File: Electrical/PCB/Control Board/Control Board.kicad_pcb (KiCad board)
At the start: 2 copper layers, 154 x 175 mm, 92 parts, among them J1 ED2627-ND, J10 6posheader, J11 S7038-ND, J13 ED1501-ND, J14 ED2989-ND-USB, J15 ED2580-ND, J16 ED2580-ND, J17 ED2744-ND, J18 ED2744-ND, J19 ED2744-ND, J2 ED2627-ND, J20 ED2744-ND, J21 ED2744-ND, J22 ED2744-ND, J23 ED2744-ND, J24 ED2744-ND, J25 ED2744-ND, J26 ED2744-ND, J28 ED2580-ND, J29 ED2580-ND, J3 ED2627-ND, J30 ED2580-ND, J31 ED2580-ND, J4 ED2627-ND, J5 ED2627-ND, J6 S9175-ND, J7 S9175-ND, J8 6posheader, J9 S7038-ND, M1 Mounting_Holes, T1 test_point, T10 test_point, T11 test_point, T12 test_point, T13 test_point, T14 test_point, T15 test_point, T16 test_point, T17 test_point, T18 test_point, T19 test_point, T2 test_point, T20 test_point, T21 test_point, T3 test_point, T4 test_point, T5 test_point, T6 test_point, T7 test_point, T8 test_point, T9 test_point, U1 LM358-N, U2 LM358-N, y1 rover_silkscreen

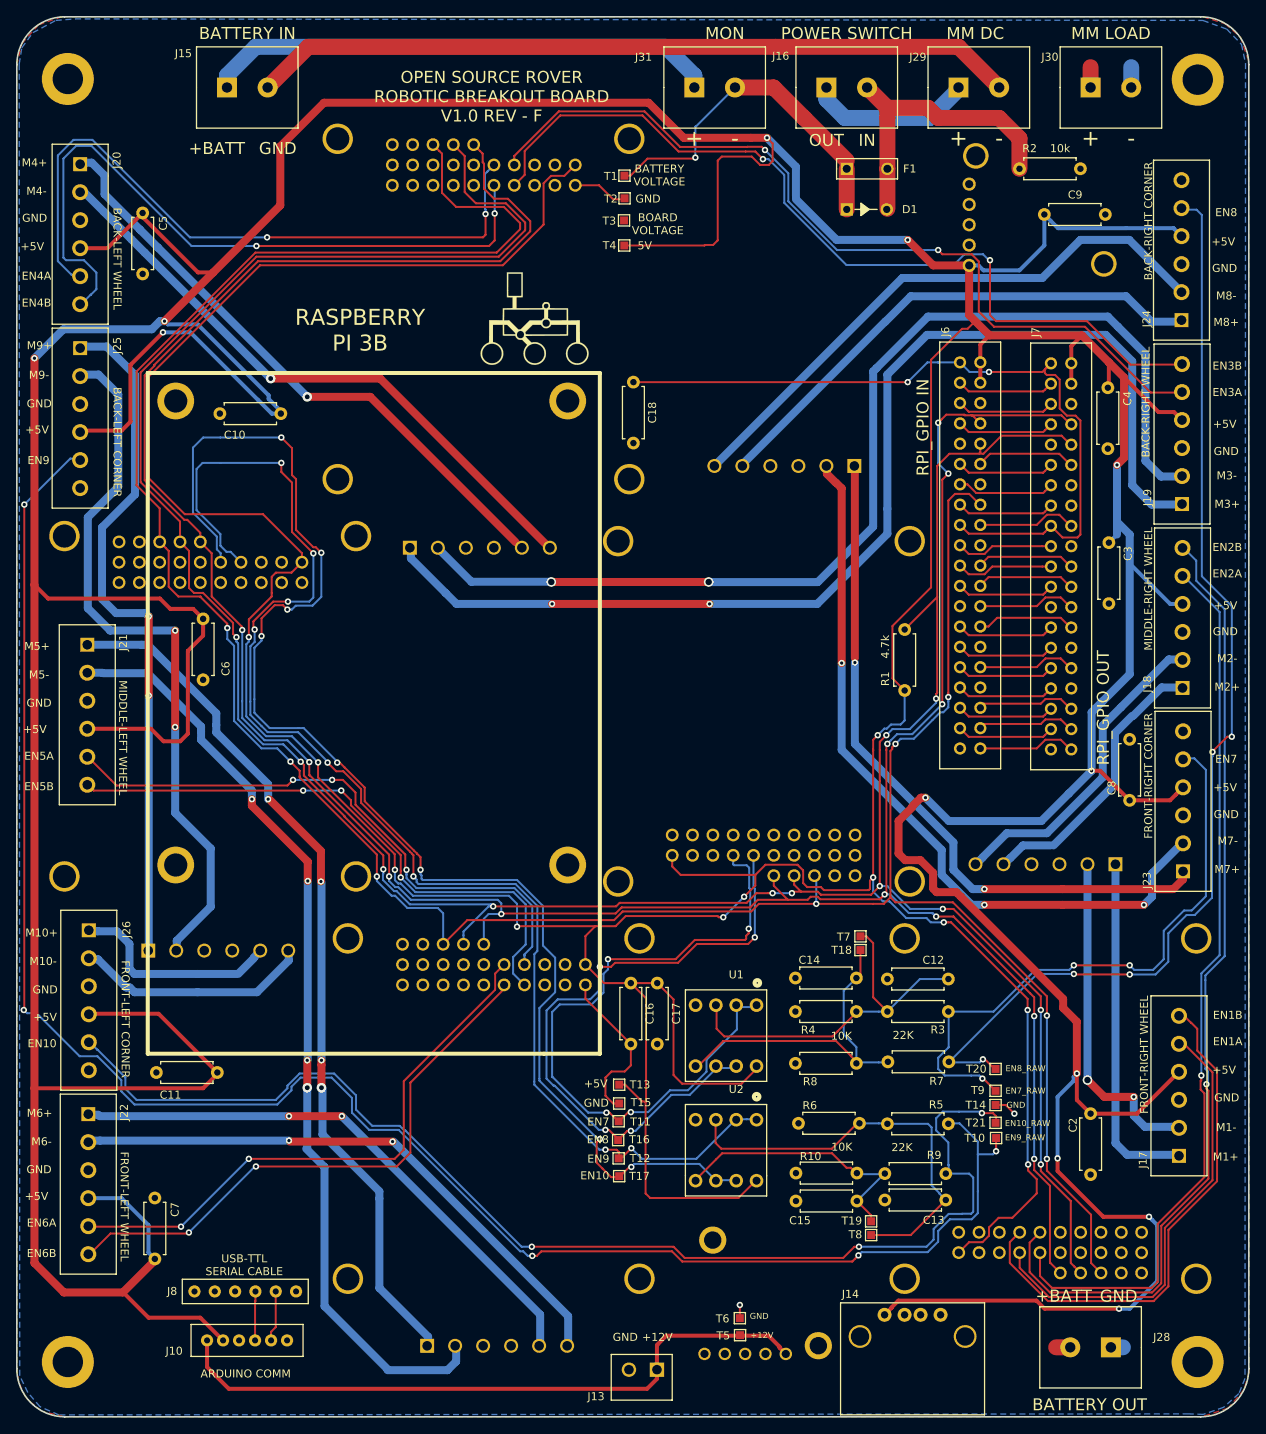
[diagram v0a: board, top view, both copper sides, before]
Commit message: Added filter caps for quadrature encoder signals
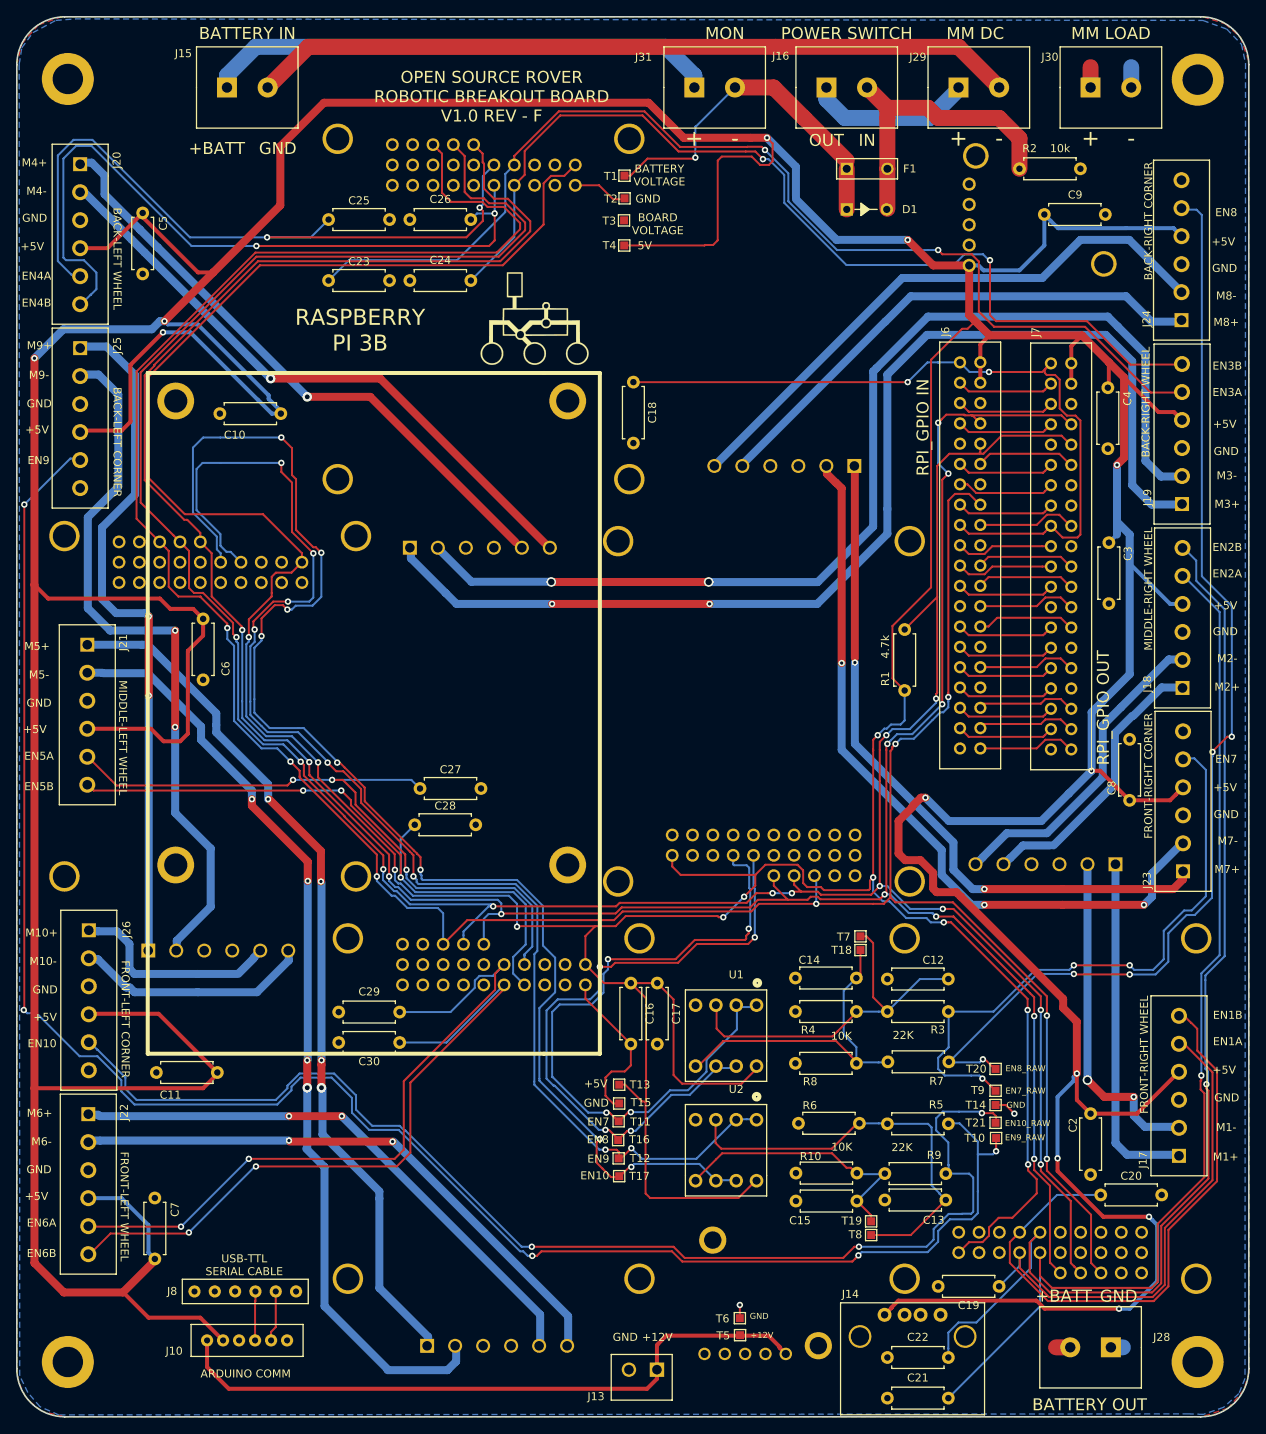
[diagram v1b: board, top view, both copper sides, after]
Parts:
- added C19: 10nf, Resistor_THT:R_Axial_DIN0207_L6.3mm_D2.5mm_P7.62mm_Horizontal, F.Cu at (121.8, -15.3)
- added C20: 10nf, Resistor_THT:R_Axial_DIN0207_L6.3mm_D2.5mm_P7.62mm_Horizontal, F.Cu at (134.5, -26.7)
- added C21: 10nf, Resistor_THT:R_Axial_DIN0207_L6.3mm_D2.5mm_P7.62mm_Horizontal, F.Cu at (115.4, -1.33)
- added C22: 10nf, Resistor_THT:R_Axial_DIN0207_L6.3mm_D2.5mm_P7.62mm_Horizontal, F.Cu at (115.4, -6.41)
- added C23: 10nf, Resistor_THT:R_Axial_DIN0207_L6.3mm_D2.5mm_P7.62mm_Horizontal, F.Cu at (38.0, -141.0)
- added C24: 10nf, Resistor_THT:R_Axial_DIN0207_L6.3mm_D2.5mm_P7.62mm_Horizontal, F.Cu at (55.8, -141.0)
- added C25: 10nf, Resistor_THT:R_Axial_DIN0207_L6.3mm_D2.5mm_P7.62mm_Horizontal, F.Cu at (38.0, -148.7)
- added C26: 10nf, Resistor_THT:R_Axial_DIN0207_L6.3mm_D2.5mm_P7.62mm_Horizontal, F.Cu at (55.8, -148.7)
- added C27: 10nf, Resistor_THT:R_Axial_DIN0207_L6.3mm_D2.5mm_P7.62mm_Horizontal, F.Cu at (49.4, -77.5)
- added C28: 10nf, Resistor_THT:R_Axial_DIN0207_L6.3mm_D2.5mm_P7.62mm_Horizontal, F.Cu at (48.7, -73.0)
- added C29: 10nf, Resistor_THT:R_Axial_DIN0207_L6.3mm_D2.5mm_P7.62mm_Horizontal, F.Cu at (46.9, -49.6)
- added C30: 10nf, Resistor_THT:R_Axial_DIN0207_L6.3mm_D2.5mm_P7.62mm_Horizontal, F.Cu at (46.9, -45.8)
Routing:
- net /RC2EN1A: track 107.3 -> 139.3 mm
- net /RC1EN2A: track 112.3 -> 135.3 mm
- net /RC1EN2B: track 121.4 -> 143.1 mm
- net /RC3EN2A: track 71.6 -> 87.7 mm
- net /RC3EN2B: track 71.2 -> 87.3 mm
- net /RC2EN1B: track 108.9 -> 123.1 mm
- net /RC1EN1B: track 65.2 -> 77.2 mm
- net /RC3EN1A: track 74.2 -> 85.6 mm
- net /RC2EN2A: track 85.7 -> 93.4 mm
- net /RC3EN1B: track 74.2 -> 81.5 mm
- net /RC1EN1A: track 56.4 -> 61.7 mm
- net /RC2EN2B: track 88.7 -> 92.0 mm
